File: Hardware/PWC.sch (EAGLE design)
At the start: 46 parts, among them IC1 DS3502, IC2 DS3502, IC3 ESPWROOM32, IC4 CP2102N-A01-GQFN24, J1 OUTPUT, J2 USB-C-16P-16P, J3 BUT5, J4 JOYSTICK, Q1 MMDT3904

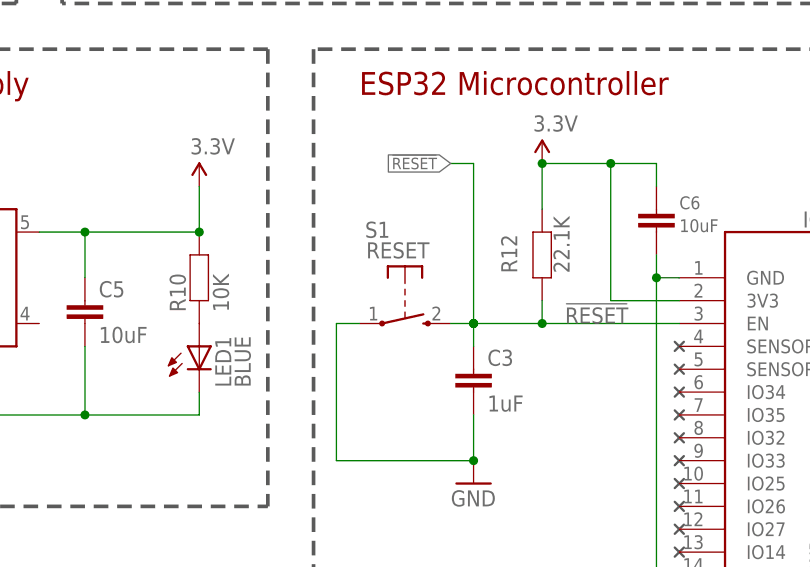
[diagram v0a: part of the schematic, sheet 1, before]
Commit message: Updated parts to use the new SuperHouse Eagle libraries.
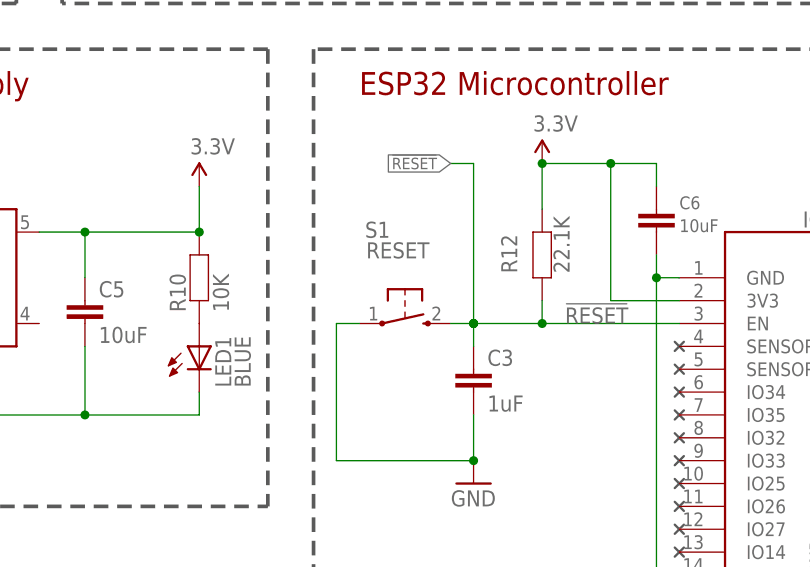
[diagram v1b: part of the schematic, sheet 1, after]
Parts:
- C1, C2, C3: device SuperHouse-DiscreteSemi:CAP0603 -> SuperHouse-Capacitors:CAP0603
- C4, C5, C6: device SuperHouse-DiscreteSemi:CAP0805 -> SuperHouse-Capacitors:CAP0805
- F1: device SuperHouse-Fuses:PTC050 -> SuperHouse-Fuses:PTC050-1812
- Q1: device SuperHouse-DiscreteSemi:TRANS_NPN_DUAL-MMDT3904 -> SuperHouse-Transistors:TRANS_NPN_DUAL-MMDT3904
- R1, R10, R11, R12, R13, R14, R15, R16, R17, R18, R19, R2, R3, R4, R5, R6, R7, R8, R9: device SuperHouse-DiscreteSemi:RESISTOR0603 -> SuperHouse-Resistors:RESISTOR0603
- Z1, Z2: device SuperHouse-DiscreteSemi:TVS0603 -> SuperHouse-Diodes:TVS0603
